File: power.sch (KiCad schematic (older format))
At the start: 19 parts, among them J1 USB_B_Micro, SW1 SW_SPDT, U101 TPS767D301-EP, U102 TLC555CP, U103 74LVC1G04

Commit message: Remove dependency on digikey libraries.
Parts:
- SW1: footprint digikey-footprints:Toggle_Switch_100SP1T2B4M6QE -> gradator:Toggle_Switch_100SP1T2B4M6QE
- U101: footprint digikey-footprints:TSSOP-28-1EP_W4.40mm -> gradator:TSSOP-28-1EP_W4.40mm
- U102: footprint digikey-footprints:SOIC-8_W3.9mm -> Package_SO:SOIC-8_3.9x4.9mm_P1.27mm; symbol dk_Clock-Timing-Programmable-Timers-and-Oscillators:TLC555CP -> gradator:TLC555CP
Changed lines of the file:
@@
 F 0 "SW1" H 2750 1575 50  0000 C CNN
 F 1 "SW_SPDT" H 2750 1666 50  0000 C CNN
-F 2 "digikey-footprints:Toggle_Switch_100SP1T2B4M6QE" H 2750 1900 50  0001 C CNN
+F 2 "gradator:Toggle_Switch_100SP1T2B4M6QE" H 2750 1900 50  0001 C CNN
 F 3 "~" H 2750 1900 50  0001 C CNN
 	1    2750 1900
@@
 	3200 1900 3400 1900
 $Comp
-L dk_Clock-Timing-Programmable-Timers-and-Oscillators:TLC555CP U102
+L gradator:TLC555CP U102
 U 1 1 604E6529
 P 6950 1550
 F 0 "U102" H 6950 1903 60  0000 C CNN
 F 1 "TLC555CP" H 6950 1797 60  0000 C CNN
-F 2 "digikey-footprints:SOIC-8_W3.9mm" H 7150 1750 60  0001 L CNN
+F 2 "Package_SO:SOIC-8_3.9x4.9mm_P1.27mm" H 7150 1750 60  0001 L CNN
 F 3 "http://www.ti.com/general/docs/suppproductinfo.tsp?distId=10&gotoUrl=http%3A%2F%2Fwww.ti.com%2Flit%2Fgpn%2Ftlc555" H 7150 1850 60  0001 L CNN
 F 4 "296-1857-5-ND" H 7150 1950 60  0001 L CNN "Digi-Key_PN"
@@
 F 0 "U101" H 4300 5115 50  0000 C CNN
 F 1 "TPS767D301-EP" H 4300 5024 50  0000 C CNN
-F 2 "digikey-footprints:TSSOP-28-1EP_W4.40mm" H 4350 5000 50  0001 C CNN
+F 2 "gradator:TSSOP-28-1EP_W4.40mm" H 4350 5000 50  0001 C CNN
 F 3 "" H 4300 4650 50  0001 C CNN
 	1    4300 4650

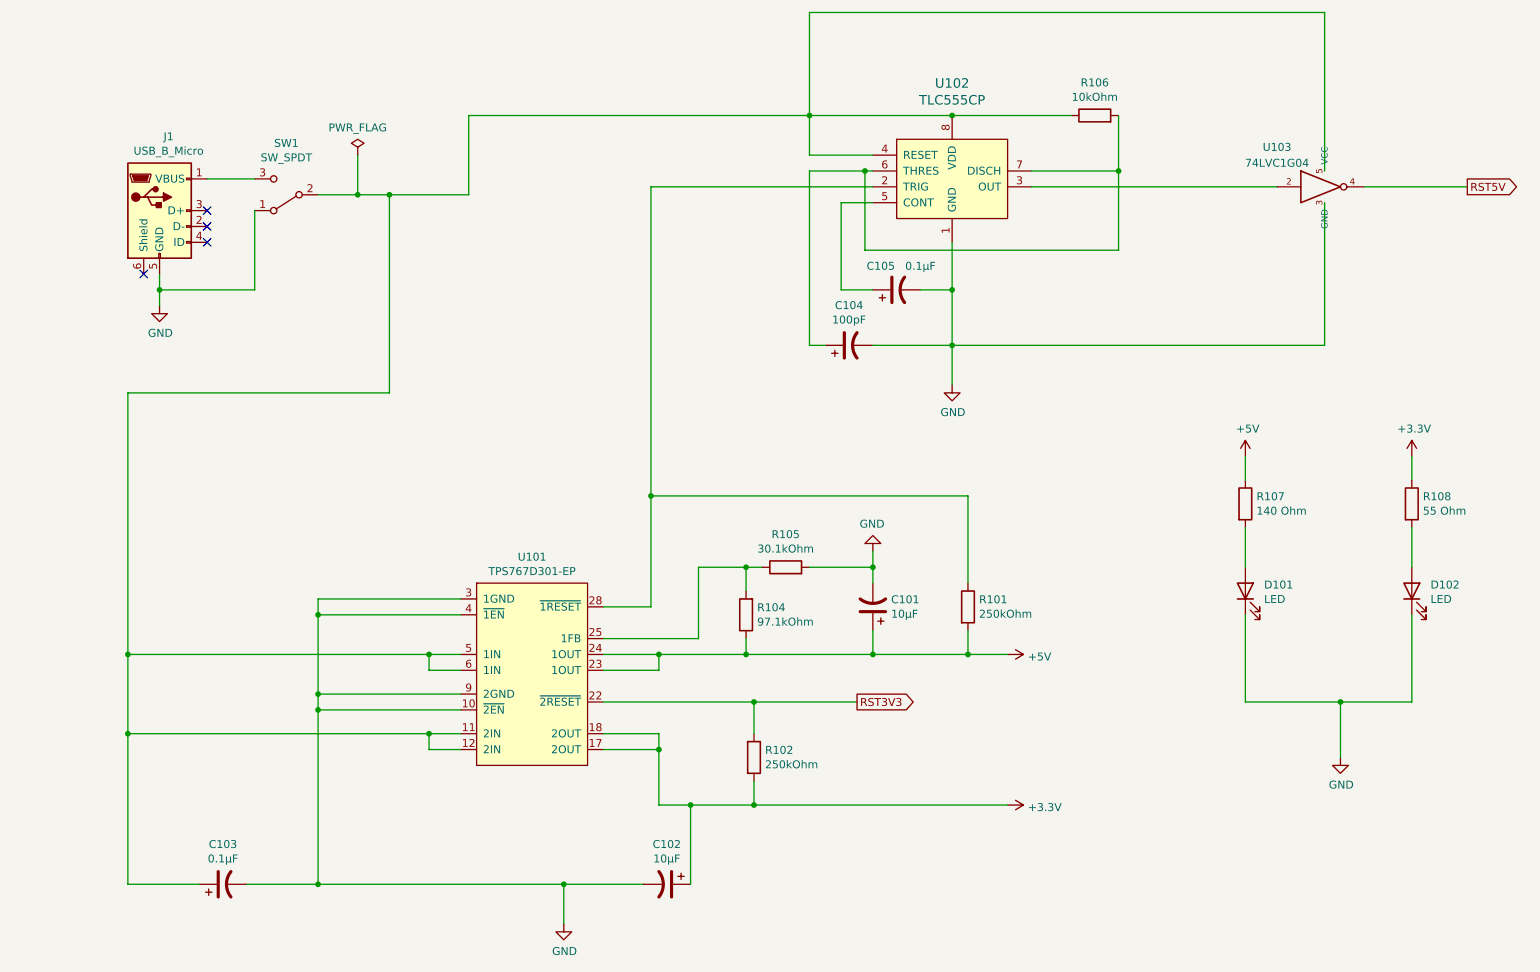
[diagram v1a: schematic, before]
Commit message: Use a zener, probably wrong knowing my electronics-fu.
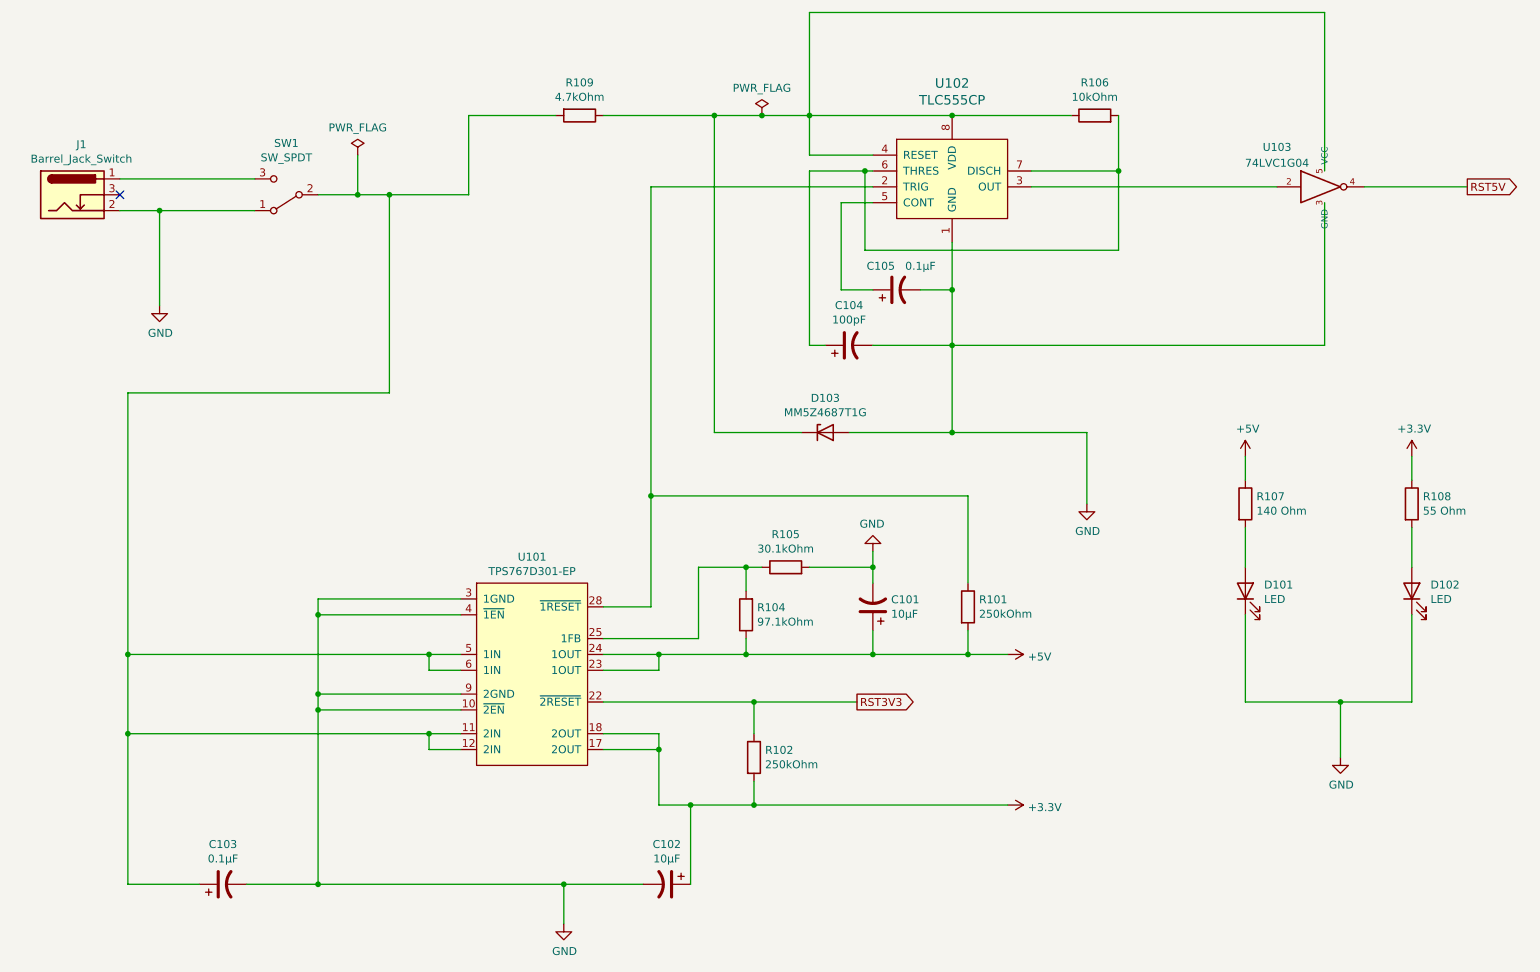
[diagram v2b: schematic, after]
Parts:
- removed J1: USB_B_Micro, gradator:USB_Micro_B_Female_0473460001, symbol Connector:USB_B_Micro
- added D103: MM5Z4687T1G, Diode_SMD:D_SOD-523, symbol Diode:MM5Zxx
- added J1: Barrel_Jack_Switch, Connector_BarrelJack:BarrelJack_CUI_PJ-102AH_Horizontal, symbol Connector:Barrel_Jack_Switch
- added R109: 4.7kOhm, symbol Device:R
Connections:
- net GND: now also D103.2 (A), J1.2
- net at C103.1, SW1.2 (B), U101.11 (2IN)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: now also R109.2; no longer R106.1, U102.4 (RESET), U102.8 (VDD), U103.5 (VCC)
- net at SW1.3 (C): now also J1.1
- new net: D103.1 (K), R106.1, R109.1, U102.4 (RESET), U102.8 (VDD), U103.5 (VCC)
- no-connect marks 4 -> 1
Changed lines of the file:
@@
 L power:GND #PWR0206
 U 1 1 604F810F
-P 6950 3100
-F 0 "#PWR0206" H 6950 2850 50  0001 C CNN
-F 1 "GND" H 6955 2927 50  0000 C CNN
-F 2 "" H 6950 3100 50  0001 C CNN
-F 3 "" H 6950 3100 50  0001 C CNN
-	1    6950 3100
+P 7800 3850
+F 0 "#PWR0206" H 7800 3600 50  0001 C CNN
+F 1 "GND" H 7805 3677 50  0000 C CNN
+F 2 "" H 7800 3850 50  0001 C CNN
+F 3 "" H 7800 3850 50  0001 C CNN
+	1    7800 3850
 	1    0    0    -1
 $EndComp
@@
 Connection ~ 6950 2850
 Wire Wire Line
-	6950 2850 6950 3100
-Wire Wire Line
 	6400 1750 6050 1750
 Wire Wire Line
@@
 Wire Wire Line
 	6050 750  9300 750
-$Comp
-L Connector:USB_B_Micro J1
-U 1 1 60231087
-P 1950 2000
-F 0 "J1" H 2007 2467 50  0000 C CNN
-F 1 "USB_B_Micro" H 2007 2376 50  0000 C CNN
-F 2 "gradator:USB_Micro_B_Female_0473460001" H 2100 1950 50  0001 C CNN
-F 3 "~" H 2100 1950 50  0001 C CNN
-	1    1950 2000
-	1    0    0    -1
-$EndComp
-NoConn ~ 1850 2400
-NoConn ~ 2250 2200
-NoConn ~ 2250 2100
-NoConn ~ 2250 2000
 Wire Wire Line
 	3900 1900 3900 1400
 Wire Wire Line
-	3900 1400 6050 1400
-Wire Wire Line
 	1750 3150 3400 3150
 Wire Wire Line
@@
 Wire Wire Line
 	3400 1900 3900 1900
-Wire Wire Line
-	1950 2600 1950 2500
 $Comp
 L power:GND #PWR0111
@@
 	2950 1900 3200 1900
 Connection ~ 3400 1900
-Wire Wire Line
-	2550 1800 2250 1800
 $Comp
 L Switch:SW_SPDT SW1
@@
 	-1   0    0    1
 $EndComp
-Wire Wire Line
-	1950 2500 2550 2500
-Wire Wire Line
-	2550 2500 2550 2000
-Connection ~ 1950 2500
-Wire Wire Line
-	1950 2500 1950 2400
 $Comp
 L power:PWR_FLAG #FLG0106
@@
 Wire Wire Line
 	9850 3700 9850 3550
+$Comp
+L Connector:Barrel_Jack_Switch J1
+U 1 1 6041A87E
+P 1400 1900
+F 0 "J1" H 1457 2217 50  0000 C CNN
+F 1 "Barrel_Jack_Switch" H 1457 2126 50  0000 C CNN
+F 2 "Connector_BarrelJack:BarrelJack_CUI_PJ-102AH_Horizontal" H 1450 1860 50  0001 C CNN
+F 3 "~" H 1450 1860 50  0001 C CNN
+	1    1400 1900
+	1    0    0    -1
+$EndComp
+Wire Wire Line
+	1950 2000 1700 2000
+Wire Wire Line
+	1950 2000 2550 2000
+Connection ~ 1950 2000
+Wire Wire Line
+	1950 2000 1950 2600
+Wire Wire Line
+	1700 1800 2550 1800
+NoConn ~ 1700 1900
+$Comp
+L Diode:MM5Zxx D103
+U 1 1 608840FF
+P 6150 3400
+F 0 "D103" H 6150 3617 50  0000 C CNN
+F 1 "MM5Z4687T1G" H 6150 3526 50  0000 C CNN
+F 2 "Diode_SMD:D_SOD-523" H 6150 3225 50  0001 C CNN
+F 3 "https://diotec.com/tl_files/diotec/files/pdf/datasheets/mm5z2v4.pdf" H 6150 3400 50  0001 C CNN
+	1    6150 3400
+	1    0    0    -1
+$EndComp
+Wire Wire Line
+	5450 3400 6000 3400
+Wire Wire Line
+	6950 2850 6950 3400
+Wire Wire Line
+	6950 3400 6300 3400
+Wire Wire Line
+	6950 3400 7800 3400
+Wire Wire Line
+	7800 3400 7800 3850
+Connection ~ 6950 3400
+Wire Wire Line
+	5450 1400 5750 1400
+Wire Wire Line
+	5450 1400 5450 3400
+$Comp
+L Device:R R109
+U 1 1 608C4BEA
+P 4600 1400
+F 0 "R109" V 4393 1400 50  0000 C CNN
+F 1 "4.7kOhm" V 4484 1400 50  0000 C CNN
+F 2 "" V 4530 1400 50  0001 C CNN
+F 3 "~" H 4600 1400 50  0001 C CNN
+	1    4600 1400
+	0    1    1    0
+$EndComp
+Wire Wire Line
+	4750 1400 5450 1400
+Connection ~ 5450 1400
+Wire Wire Line
+	3900 1400 4450 1400
+$Comp
+L power:PWR_FLAG #FLG0107
+U 1 1 608D3E1A
+P 5750 1400
+F 0 "#FLG0107" H 5750 1475 50  0001 C CNN
+F 1 "PWR_FLAG" H 5750 1573 50  0000 C CNN
+F 2 "" H 5750 1400 50  0001 C CNN
+F 3 "~" H 5750 1400 50  0001 C CNN
+	1    5750 1400
+	1    0    0    -1
+$EndComp
+Connection ~ 5750 1400
+Wire Wire Line
+	5750 1400 6050 1400
 $EndSCHEMATC
